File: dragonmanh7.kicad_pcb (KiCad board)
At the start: 4 copper layers, 135.6 x 54.6 mm, 146 parts, among them J1 USB_B, J10 Conn_02x12_Odd_Even, J11 Conn_02x05_Odd_Even, J12 VBAT+, J13 Conn_02x05_Odd_Even, J14 VBATG, J15 Conn_02x02_Odd_Even, J16 Conn_02x02_Odd_Even, J18 Conn_02x05_Odd_Even, J2 73725-0110BLF, J3 RJ45_Amphenol_RJMG1BD3B8K1ANR, J4 105162-0001, J5 Screw_Terminal_01x06, J6 Conn_02x12_Odd_Even, J7 USB_B, J8 Screw_Terminal_01x02, J9 Conn_02x12_Odd_Even, SW1 RESET, SW2 PC13, U1 STM32H743VITx, U10 USBLC6-2SC6, U12 TCAN332, U13 ISL83483, U14 MIC2005A, U2 LAN8742A-CZ-TR, U3 AZ1117CD-3.3TRG1, U5 S25FL127SABMFI101, U6 AP63205, U7 USBLC6-2SC6, U8 STM32F042F6Px, U9 USBLC6-2SC6, Y1 8MHz, Y2 32.768KHz, Y3 25MHz

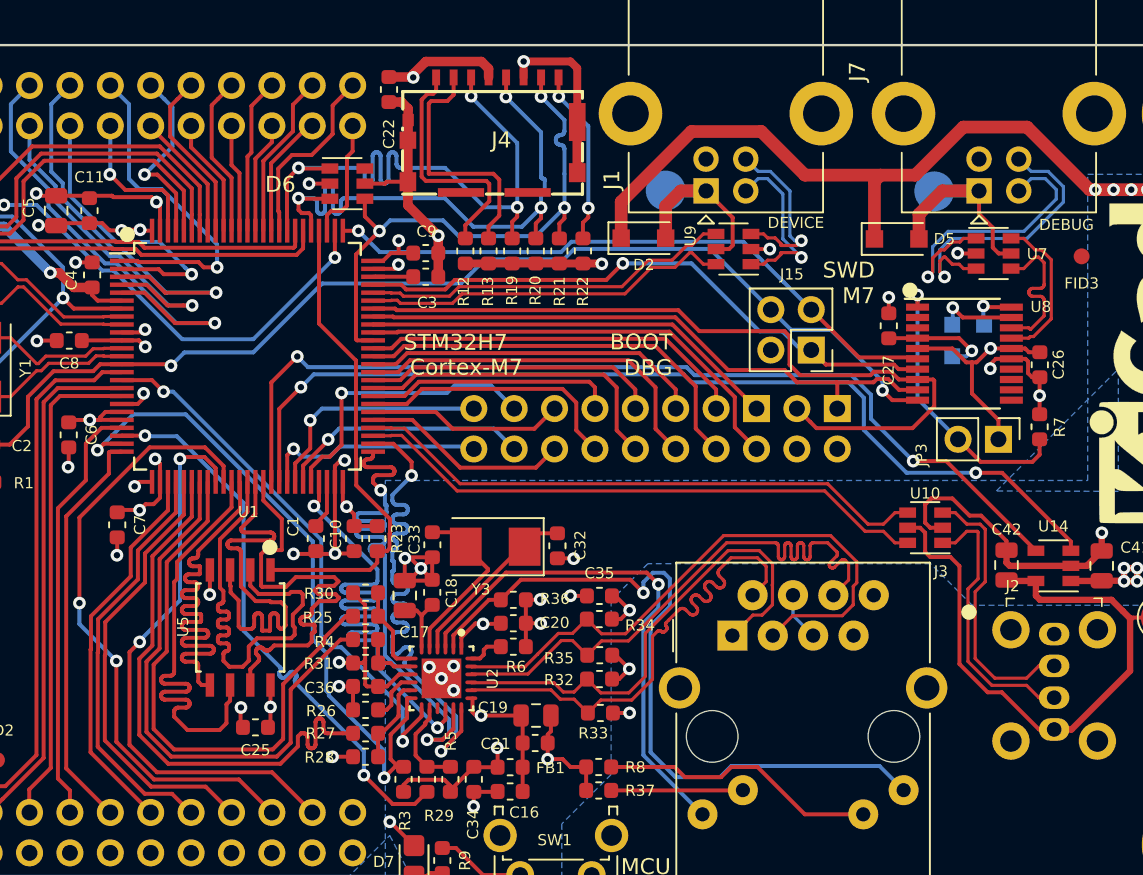
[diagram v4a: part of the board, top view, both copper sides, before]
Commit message: Minor changes, add uSD DET on PC10
Signed-off-by: Martin Ribelotta <martinribelotta@gmail.com>
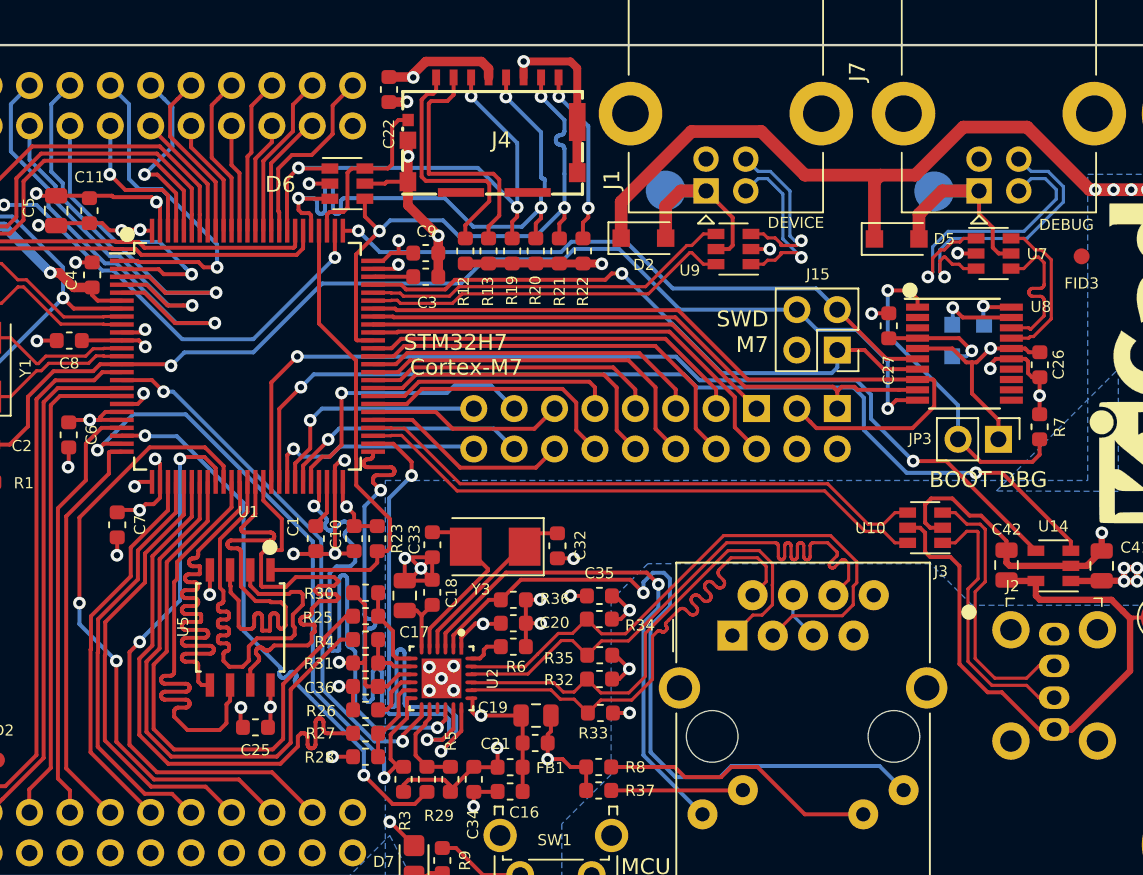
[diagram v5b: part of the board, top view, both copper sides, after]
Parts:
- U5: value S25FL127SABMFI101 -> W25Q32JVSSIQ
- moved J15 1.64 mm to (167.6, 47.1)
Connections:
- D6 pad 6: (no net) -> /PC10
- J4 pad 9: GND -> /PC10
- J9 pad 23: /PC10 -> GND
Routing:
- net /SDMMC_CMD: track 39.3 -> 32.5 mm
- net /PC10: track 7.65 -> 11.3 mm
- net /BOOT0_B: track 17.8 -> 20.7 mm
- net GND: track 215.7 -> 213.6 mm, vias 55 -> 58
- net /~RESET: track 140.9 -> 142.7 mm
- net /SWDIO: track 37.8 -> 39.1 mm
- net /U1_RX: track 49.7 -> 48.5 mm
- net /ENET_MDC: track 34.3 -> 35.0 mm
- net /U1_TX: track 38.0 -> 37.5 mm

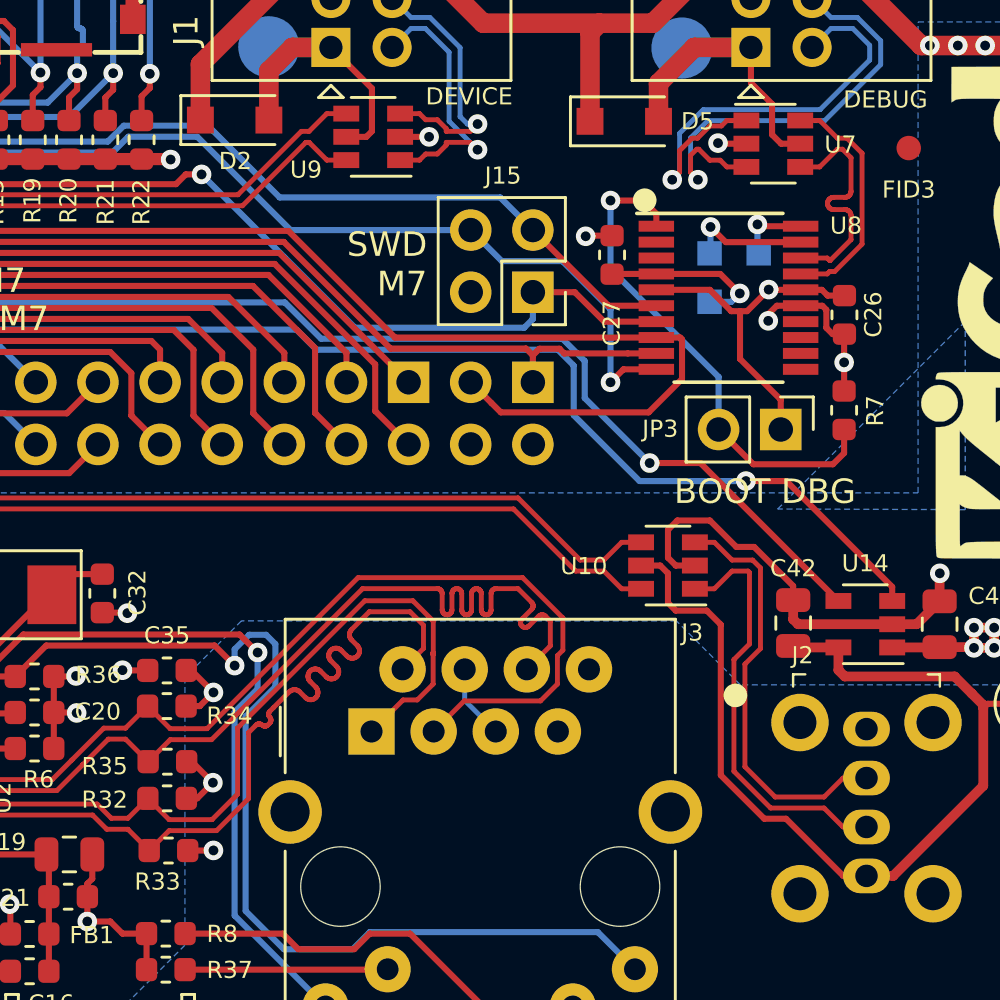
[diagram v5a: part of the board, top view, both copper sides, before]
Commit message: ETH and usb skew near of unmatched area
Signed-off-by: Martin Ribelotta <martinribelotta@gmail.com>
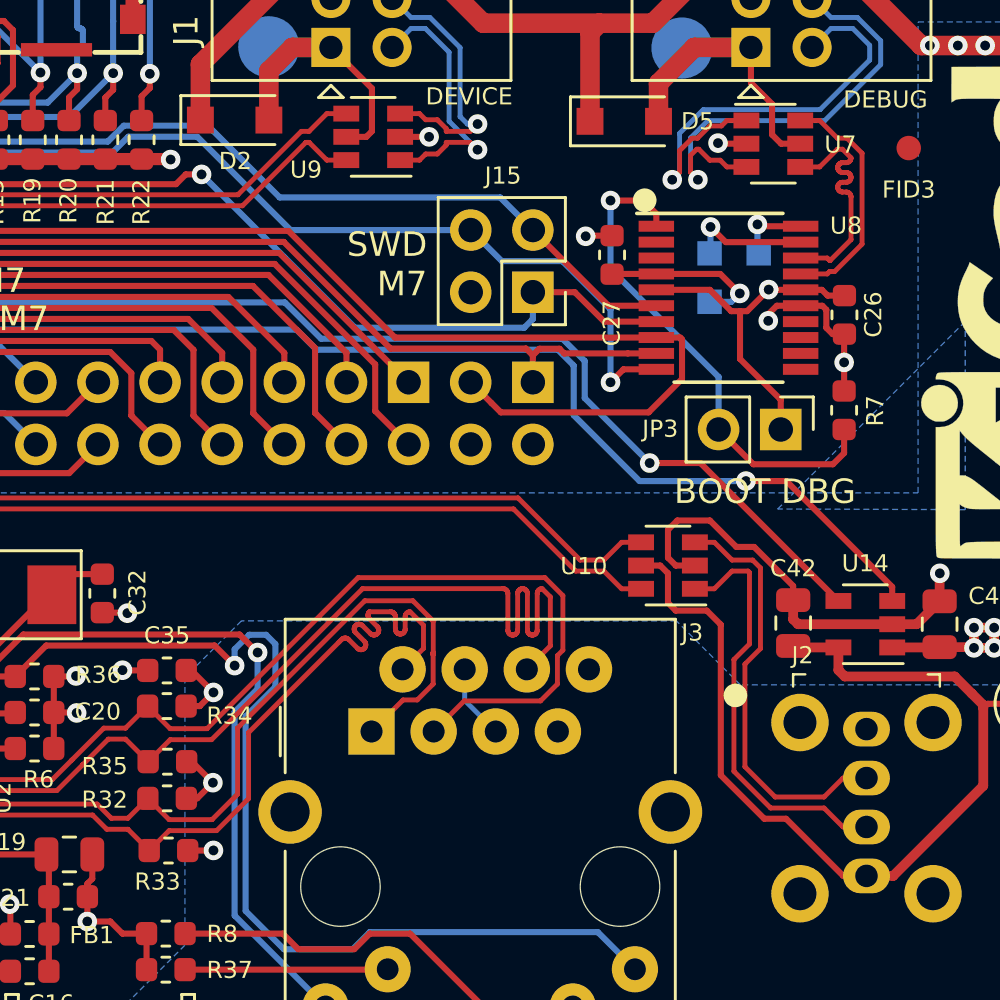
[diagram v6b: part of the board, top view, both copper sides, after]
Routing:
- net /RD+: track 37.8 -> 38.3 mm
- net /RD-: track 37.8 -> 38.3 mm

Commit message: Point of restoration
Signed-off-by: Martin Ribelotta <martinribelotta@gmail.com>
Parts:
- removed C4: 0.1u, Capacitor_SMD:C_0603_1608Metric
- removed J14: VBATG, TestPoint:TestPoint_Loop_D1.80mm_Drill1.0mm_Beaded
- removed JP5: Jumper_2_Bridged, Jumper:SolderJumper-2_P1.3mm_Bridged_RoundedPad1.0x1.5mm
- removed TP1: VBAT_TP, TestPoint:TestPoint_Pad_D2.5mm
- added BT1: MS621F-FL11E, Battery:BatteryHolder_Seiko_MS621F, F.Cu at (104.9, 51.6)
- added D11: MBR120VLSFT3G, Diode_SMD:D_SOD-123F, F.Cu at (107.4, 47.7)
- added D9: MBR120VLSFT3G, Diode_SMD:D_SOD-123F, F.Cu at (107.4, 52.2)
- added JP4: Jumper_2_Bridged, Jumper:SolderJumper-2_P1.3mm_Open_RoundedPad1.0x1.5mm, B.Cu at (111.1, 36.0)
- added R38: 220R, Resistor_SMD:R_0603_1608Metric, F.Cu at (105.3, 47.5)
- J12: value VBAT+ -> VBAT
- moved R7 8.51 mm to (171.9, 52.7), turned to 0 degrees
- moved J12 3.41 mm to (107.4, 43.6)
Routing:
- net Net-(BT1-Pad1): track 0.00 -> 6.63 mm
- net /BOOT0_B: track 20.7 -> 16.4 mm
- net GND: track 213.6 -> 217.3 mm, vias 58 -> 57
- net /CAN_TX: track 68.5 -> 71.7 mm
- net /CAN_RX: track 66.4 -> 69.5 mm
- net +3V3: track 172.8 -> 175.8 mm
- net /RS485_DE: track 60.2 -> 62.3 mm
- net /RS485_TX: track 46.4 -> 45.9 mm
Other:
- board text added: "+VBAT"
- board text removed: "+"
- board text removed: "-"
- board text removed: "VBAT 3V"
